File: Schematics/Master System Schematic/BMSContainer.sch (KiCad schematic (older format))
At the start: 2 parts, among them U1 OrionBMS2v2, U2 OrionThermExp

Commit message: Revert "Zack BMS Edits"
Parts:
- removed U1: OrionBMS2v2, symbol NER:OrionBMS2v2
- added U1: OrionBMS2, symbol NER:OrionBMS2
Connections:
- net labels added: ChargeSafety, GLV
- net labels removed: ChargerSafety, GLV+
- wire segments 80 -> 77
- no-connect marks 29 -> 2

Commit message: FIXED IT MANUALLY
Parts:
- removed U1: OrionBMS2, symbol NER:OrionBMS2
- added U1: OrionBMS2v2, symbol NER:OrionBMS2v2
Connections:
- net labels added: ChargerSafety, GLV+
- net labels removed: ChargeSafety, GLV
- wire segments 77 -> 80
- no-connect marks 2 -> 29

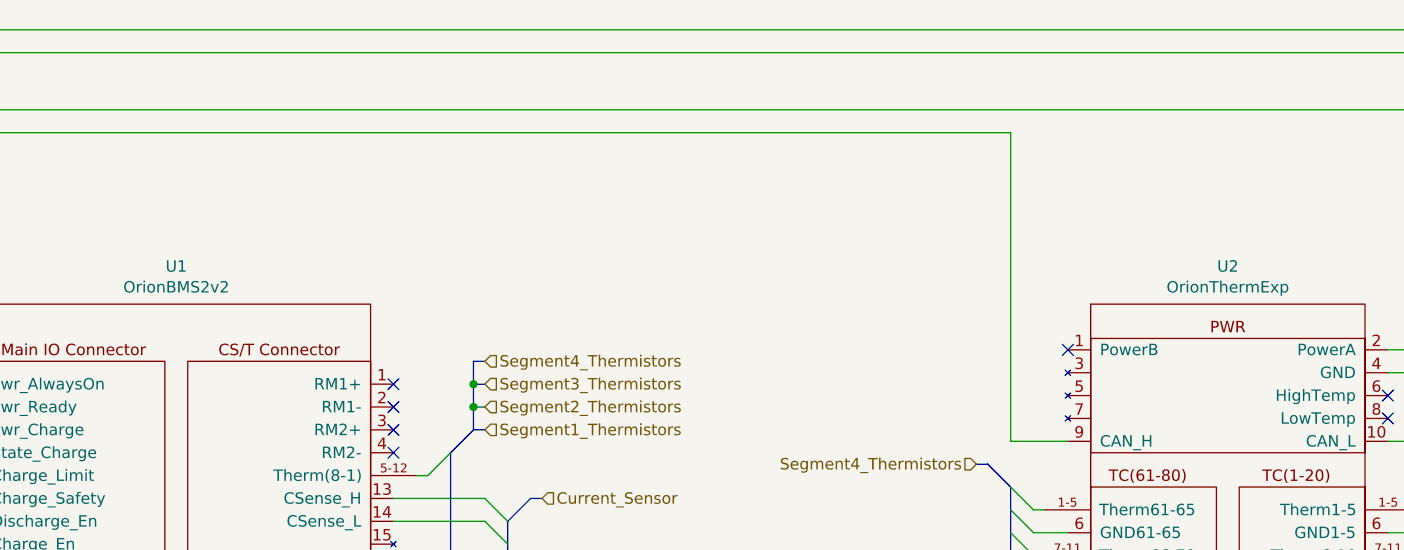
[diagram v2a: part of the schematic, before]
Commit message: Had to refactor all IDs
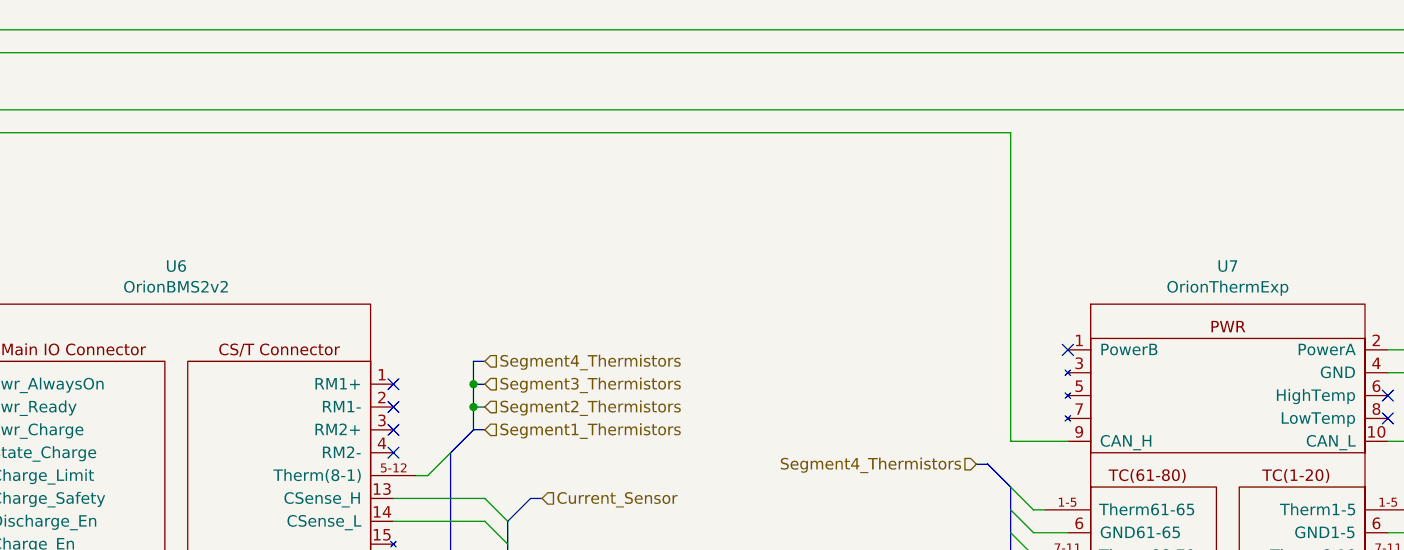
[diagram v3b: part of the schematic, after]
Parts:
- renumbered U1 to U6, U2 to U7
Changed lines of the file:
@@
 $Descr A 11000 8500
 encoding utf-8
-Sheet 4 17
+Sheet 4 21
 Title "BMS Container"
 Date "2020-10-16"
@@
 NoConn ~ 7200 2100
 $Comp
-L NER:OrionThermExp U2
+L NER:OrionThermExp U7
 U 1 1 5F8ADC5C
 P 7900 1900
-F 0 "U2" H 7900 2065 50  0000 C CNN
+F 0 "U7" H 7900 2065 50  0000 C CNN
 F 1 "OrionThermExp" H 7900 1974 50  0000 C CNN
 F 2 "" H 7900 1800 50  0001 C CNN
@@
 	4500 2550 4500 3250
 $Comp
-L NER:OrionBMS2v2 U1
+L NER:OrionBMS2v2 U6
 U 1 1 5F91103C
 P 3300 3100
-F 0 "U1" H 3300 4465 50  0000 C CNN
+F 0 "U6" H 3300 4465 50  0000 C CNN
 F 1 "OrionBMS2v2" H 3300 4374 50  0000 C CNN
 F 2 "" H 3300 4400 50  0001 C CNN

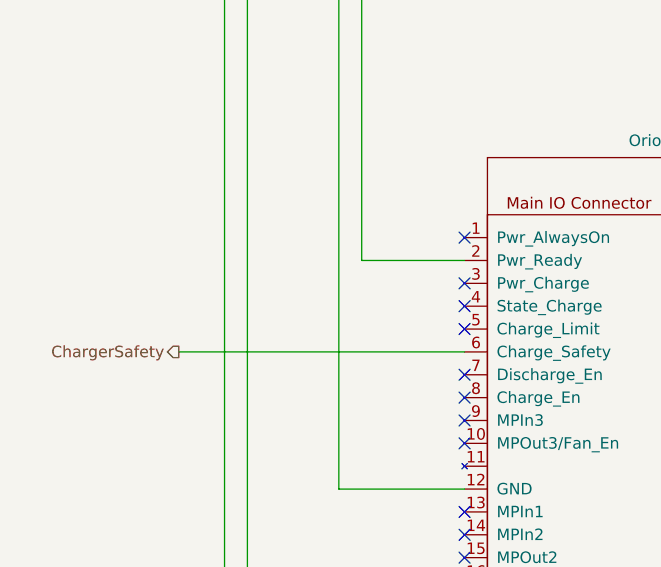
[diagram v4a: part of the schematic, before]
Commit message: Added Charger Power pin to BMS schem
Pulled charger power pin through to master sheet.
Not implemented because I'm not sure how david will be doing this
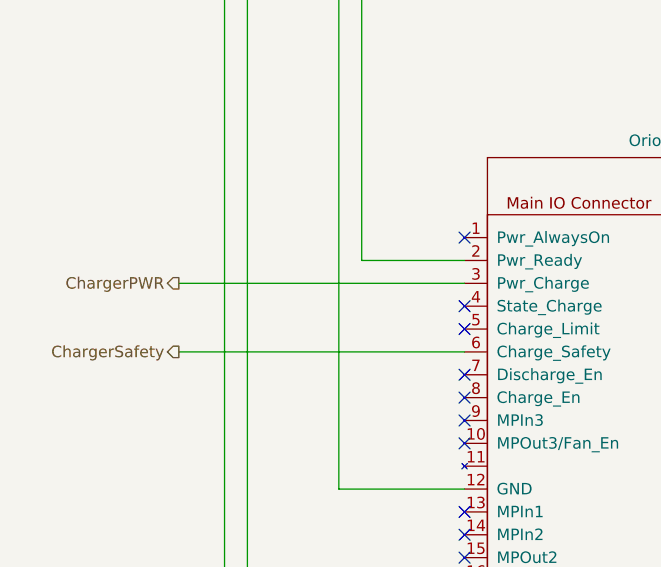
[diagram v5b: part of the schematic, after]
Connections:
- net ChargerPWR: now reaches U6.3 (RM2+)
- no-connect marks 29 -> 28
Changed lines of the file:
@@
 $EndComp
 NoConn ~ 2350 2250
-NoConn ~ 2350 2450
 NoConn ~ 2350 2550
 NoConn ~ 2350 2650
@@
 Wire Wire Line
 	1900 4750 2350 4750
+Text HLabel 1100 2450 0    50   Output ~ 0
+ChargerPWR
+Wire Wire Line
+	1100 2450 2350 2450
 Wire Bus Line
 	4500 4000 4500 4300

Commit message: Fixed BMSContainer component
Added 2 connectors and fixed wiring
Updated annotations
Updated version
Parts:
- U6: symbol NER:OrionBMS2v2 -> NER:OrionBMS2
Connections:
- no-connect marks 28 -> 30
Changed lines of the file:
@@
 EESchema Schematic File Version 4
-LIBS:Master System Schematic-cache
 EELAYER 30 0
 EELAYER END
 $Descr A 11000 8500
 encoding utf-8
-Sheet 4 21
+Sheet 1 1
 Title "BMS Container"
-Date "2020-10-16"
-Rev "1"
+Date "2020-10-22"
+Rev "1.1"
 Comp "Northeaster Electric Racing"
 Comment1 "Dylan Gardner, Zack Perry"
@@
 Text HLabel 4900 2750 2    50   Input ~ 0
 Current_Sensor
-Text HLabel 4650 5200 2    50   Input ~ 0
+Text HLabel 4650 5950 2    50   Input ~ 0
 Segment3_VoltageTaps
-Text HLabel 4650 4300 2    50   Input ~ 0
+Text HLabel 4650 5000 2    50   Input ~ 0
 Segment2_VoltageTaps
-Text HLabel 4650 3900 2    50   Input ~ 0
-Segment1_VoltageTaps
-Entry Wire Line
-	4400 4100 4500 4000
-Entry Wire Line
-	4400 4200 4500 4100
-Entry Wire Line
-	4400 4300 4500 4200
-Entry Wire Line
-	4400 4400 4500 4300
-Entry Wire Line
-	4400 4500 4500 4400
-Entry Wire Line
-	4400 4600 4500 4500
-Entry Wire Line
-	4400 5200 4500 5100
-Entry Wire Line
-	4400 5300 4500 5200
-Entry Wire Line
-	4400 5400 4500 5300
-Entry Wire Line
-	4400 5500 4500 5400
-Entry Wire Line
-	4400 5600 4500 5500
-Entry Wire Line
-	4400 5700 4500 5600
-Entry Bus Bus
-	4500 4000 4600 3900
-Wire Bus Line
-	4600 3900 4650 3900
-Wire Wire Line
-	4350 4100 4400 4100
-Wire Wire Line
-	4250 4200 4400 4200
-Wire Wire Line
-	4350 4300 4400 4300
-Wire Wire Line
-	4250 4400 4400 4400
-Wire Wire Line
-	4350 4500 4400 4500
-Wire Wire Line
-	4400 4600 4250 4600
-Wire Wire Line
-	4400 5200 4350 5200
-Wire Wire Line
-	4400 5300 4250 5300
-Entry Bus Bus
-	4500 4400 4600 4300
-Wire Bus Line
-	4600 4300 4650 4300
-Entry Bus Bus
-	4500 5300 4600 5200
-Wire Bus Line
-	4600 5200 4650 5200
-Wire Wire Line
-	4350 5400 4400 5400
-Wire Wire Line
-	4250 5500 4400 5500
-Wire Wire Line
-	4400 5600 4350 5600
-Wire Wire Line
-	4250 5700 4400 5700
+Entry Wire Line
+	4400 6250 4500 6150
+Entry Wire Line
+	4400 6350 4500 6250
+Entry Wire Line
+	4400 6450 4500 6350
+Wire Bus Line
+	4600 5950 4650 5950
+Wire Wire Line
+	4350 6150 4400 6150
+Wire Wire Line
+	4250 6250 4400 6250
+Wire Wire Line
+	4400 6350 4350 6350
+Wire Wire Line
+	4250 6450 4400 6450
 Wire Wire Line
 	2250 5400 2200 5400
@@
 NoConn ~ 2350 4450
 NoConn ~ 2350 4550
-NoConn ~ 2250 5600
-NoConn ~ 2350 5700
 Wire Wire Line
 	1100 1050 1400 1050
@@
 Wire Bus Line
 	4500 2550 4500 3250
+Wire Wire Line
+	4250 2850 4650 2850
+Wire Wire Line
+	4250 2750 4650 2750
+Wire Wire Line
+	4250 3550 4650 3550
+Entry Wire Line
+	4650 2750 4750 2850
+Entry Wire Line
+	4650 2850 4750 2950
+Entry Wire Line
+	4650 3450 4750 3350
+Entry Wire Line
+	4650 3550 4750 3450
+Wire Wire Line
+	1800 3350 2350 3350
+Wire Wire Line
+	1900 2350 2350 2350
+Wire Wire Line
+	9050 700  9050 2200
+Wire Wire Line
+	1100 800  1900 800
+Wire Wire Line
+	1100 700  1800 700
+Wire Wire Line
+	1900 2350 1900 800
+Connection ~ 1900 800
+Wire Wire Line
+	1800 3350 1800 700
+Connection ~ 1800 700
+Connection ~ 1300 1150
+Wire Wire Line
+	6950 1150 6950 2500
+Wire Wire Line
+	6950 2500 7200 2500
+Wire Wire Line
+	1300 1150 6950 1150
+Connection ~ 1400 1050
+Wire Wire Line
+	8850 1050 1400 1050
+Wire Wire Line
+	8850 1050 8850 2500
+Wire Wire Line
+	9050 2200 8600 2200
+Wire Wire Line
+	8600 2100 8950 2100
+Wire Wire Line
+	8950 800  8950 2100
+Wire Wire Line
+	1900 800  8950 800
+Wire Wire Line
+	1800 700  9050 700
+Text HLabel 1100 2750 0    50   Output ~ 0
+ChargerSafety
+Wire Wire Line
+	1100 2750 2350 2750
+Wire Wire Line
+	1900 4750 2350 4750
+Text HLabel 1100 2450 0    50   Output ~ 0
+ChargerPWR
+Wire Wire Line
+	1100 2450 2350 2450
 $Comp
-L NER:OrionBMS2v2 U6
+L NER:OrionBMS2 U6
 U 1 1 5F91103C
 P 3300 3100
@@
 	1    0    0    -1
 $EndComp
-Wire Wire Line
-	4250 2850 4650 2850
-Wire Wire Line
-	4250 2750 4650 2750
-Wire Wire Line
-	4250 3550 4650 3550
-Entry Wire Line
-	4650 2750 4750 2850
-Entry Wire Line
-	4650 2850 4750 2950
-Entry Wire Line
-	4650 3450 4750 3350
-Entry Wire Line
-	4650 3550 4750 3450
-Wire Wire Line
-	1800 3350 2350 3350
-Wire Wire Line
-	1900 2350 2350 2350
-Wire Wire Line
-	9050 700  9050 2200
-Wire Wire Line
-	1100 800  1900 800
-Wire Wire Line
-	1100 700  1800 700
-Wire Wire Line
-	1900 2350 1900 800
-Connection ~ 1900 800
-Wire Wire Line
-	1800 3350 1800 700
-Connection ~ 1800 700
-Connection ~ 1300 1150
-Wire Wire Line
-	6950 1150 6950 2500
-Wire Wire Line
-	6950 2500 7200 2500
-Wire Wire Line
-	1300 1150 6950 1150
-Connection ~ 1400 1050
-Wire Wire Line
-	8850 1050 1400 1050
-Wire Wire Line
-	8850 1050 8850 2500
-Wire Wire Line
-	9050 2200 8600 2200
-Wire Wire Line
-	8600 2100 8950 2100
-Wire Wire Line
-	8950 800  8950 2100
-Wire Wire Line
-	1900 800  8950 800
-Wire Wire Line
-	1800 700  9050 700
-Text HLabel 1100 2750 0    50   Output ~ 0
-ChargerSafety
-Wire Wire Line
-	1100 2750 2350 2750
-Wire Wire Line
-	1900 4750 2350 4750
-Text HLabel 1100 2450 0    50   Output ~ 0
-ChargerPWR
-Wire Wire Line
-	1100 2450 2350 2450
-Wire Bus Line
-	4500 4000 4500 4300
-Wire Bus Line
-	4500 4400 4500 5200
-Wire Bus Line
-	4500 5300 4500 5600
+Wire Bus Line
+	4600 4050 4650 4050
+Entry Bus Bus
+	4500 4150 4600 4050
+Text HLabel 4650 4050 2    50   Input ~ 0
+Segment1_VoltageTaps
+Wire Wire Line
+	4250 4350 4400 4350
+Wire Wire Line
+	4250 4550 4400 4550
+Wire Wire Line
+	4350 4450 4400 4450
+Wire Wire Line
+	4350 4250 4400 4250
+Entry Wire Line
+	4400 4550 4500 4450
+Entry Wire Line
+	4400 4450 4500 4350
+Entry Wire Line
+	4400 4350 4500 4250
+Entry Wire Line
+	4400 4250 4500 4150
+Wire Bus Line
+	4600 5000 4650 5000
+Entry Bus Bus
+	4500 5100 4600 5000
+Entry Wire Line
+	4400 6150 4500 6050
+Entry Bus Bus
+	4500 6050 4600 5950
+NoConn ~ 2250 6150
+NoConn ~ 2350 6250
+NoConn ~ 2250 6350
+NoConn ~ 2350 6450
+Wire Wire Line
+	4250 5300 4400 5300
+Wire Wire Line
+	4250 5500 4400 5500
+Wire Wire Line
+	4350 5400 4400 5400
+Wire Wire Line
+	4350 5200 4400 5200
+Entry Wire Line
+	4400 5500 4500 5400
+Entry Wire Line
+	4400 5400 4500 5300
+Entry Wire Line
+	4400 5300 4500 5200
+Entry Wire Line
+	4400 5200 4500 5100
+Wire Bus Line
+	4500 6050 4500 6350
 Wire Bus Line
 	2100 5100 2100 5400
@@
 	4750 2850 4750 3450
 Wire Bus Line
+	4500 4150 4500 4450
+Wire Bus Line
+	4500 5100 4500 5400
+Wire Bus Line
 	8850 2700 8850 3400

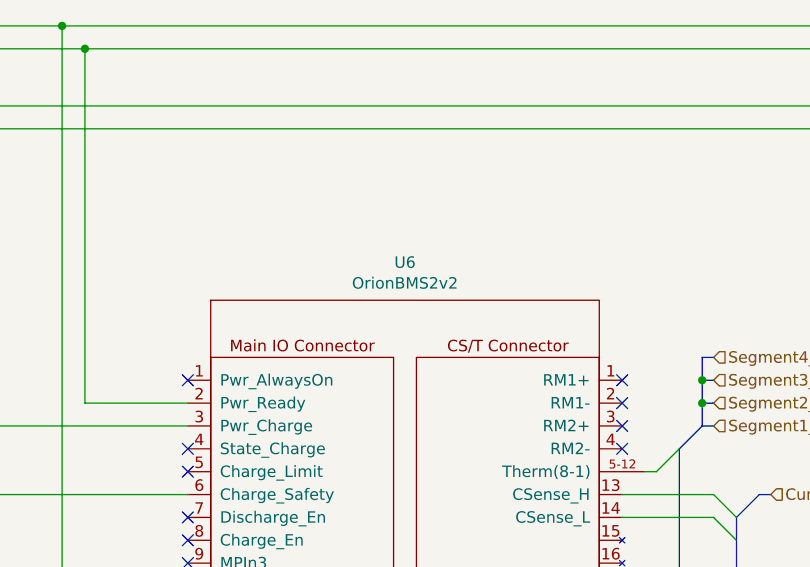
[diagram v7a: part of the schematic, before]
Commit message: Fixed name of BMS2
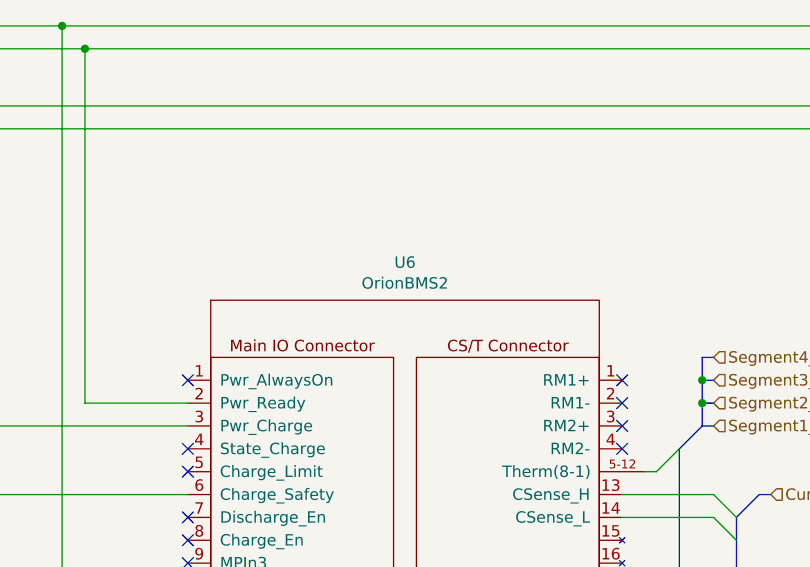
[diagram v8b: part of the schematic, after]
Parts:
- U6: value OrionBMS2v2 -> OrionBMS2
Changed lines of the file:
@@
 P 3300 3100
 F 0 "U6" H 3300 4465 50  0000 C CNN
-F 1 "OrionBMS2v2" H 3300 4374 50  0000 C CNN
+F 1 "OrionBMS2" H 3300 4374 50  0000 C CNN
 F 2 "" H 3300 4400 50  0001 C CNN
 F 3 "" H 3300 4400 50  0001 C CNN
